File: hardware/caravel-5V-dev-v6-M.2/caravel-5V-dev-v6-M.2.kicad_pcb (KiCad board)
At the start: 2 copper layers, 76.2 x 73.8 mm, 75 parts, among them J1 USB_B_Micro - 10118193-0001LF, J10 Conn_01x02_Male, J11 Conn_01x20_Female, J12 Conn_01x27_Female, J13 Conn_01x02_Male, J2 Conn_01x02_Female, J3 Conn_01x02_Male, J4 Conn_01x03_Female, J5 Conn_01x02_Male, J6 Conn_01x02_Male, J7 Conn_01x06_Female, J8 Conn_01x02_Male, J9 Conn_01x02_Male, SW1 SW_Push - SKQGADE010, T1 Logo, T2 Logo, U1 FT232H, U10 TXB0104PWR, U2 SN74LVC1G125DCKR, U3 SN74LVC1G125DCKR, U4 MCP1319MT-29LE-OT, U5 TAR5SxxU_SOT353F, U6 TXB0104PWR, U7 W25Q32FVSS, U8 caravel-M.2-card, U9 TXB0104PWR, X1 SG7050CCN_10MHZ, Y1 CSTNE12M0GH5L000R0

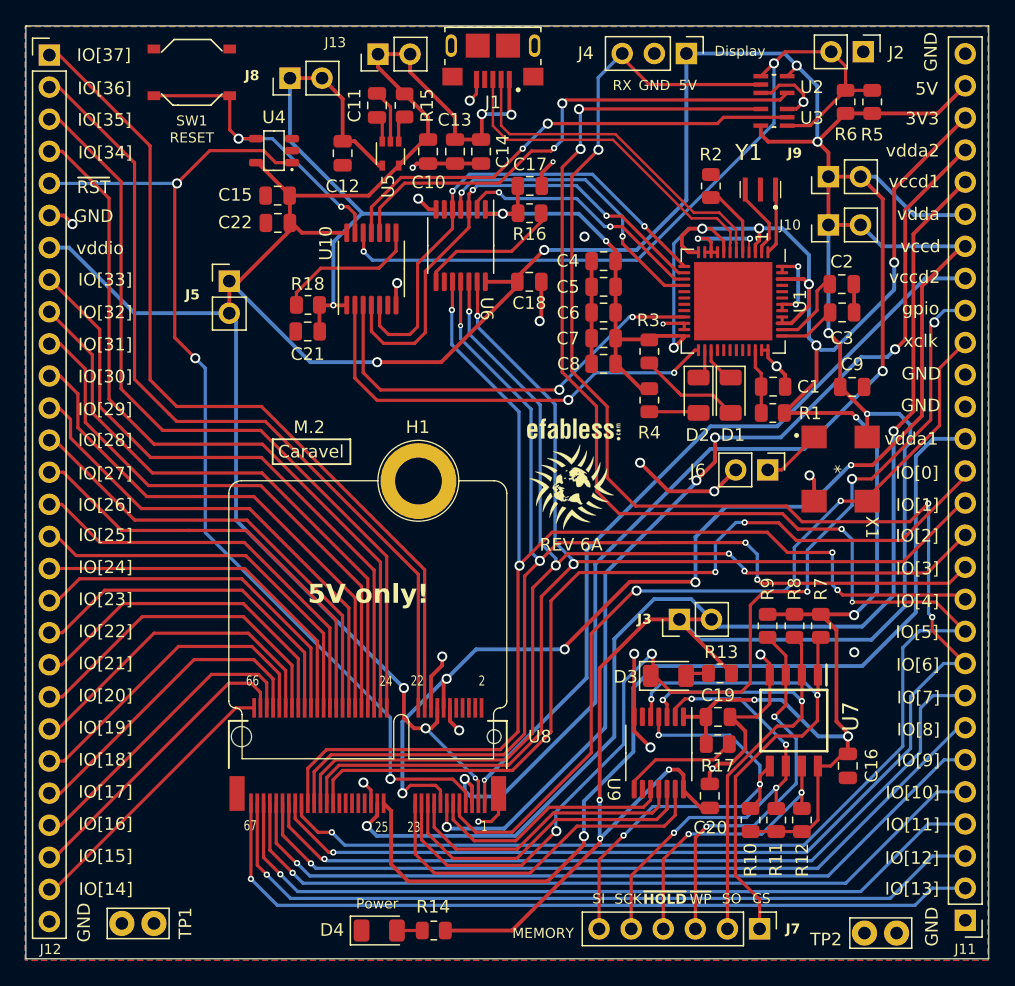
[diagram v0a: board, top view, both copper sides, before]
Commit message: update `caravel-5V-dev-v6-M.2` to REV6B that fixes identified issues during bringup
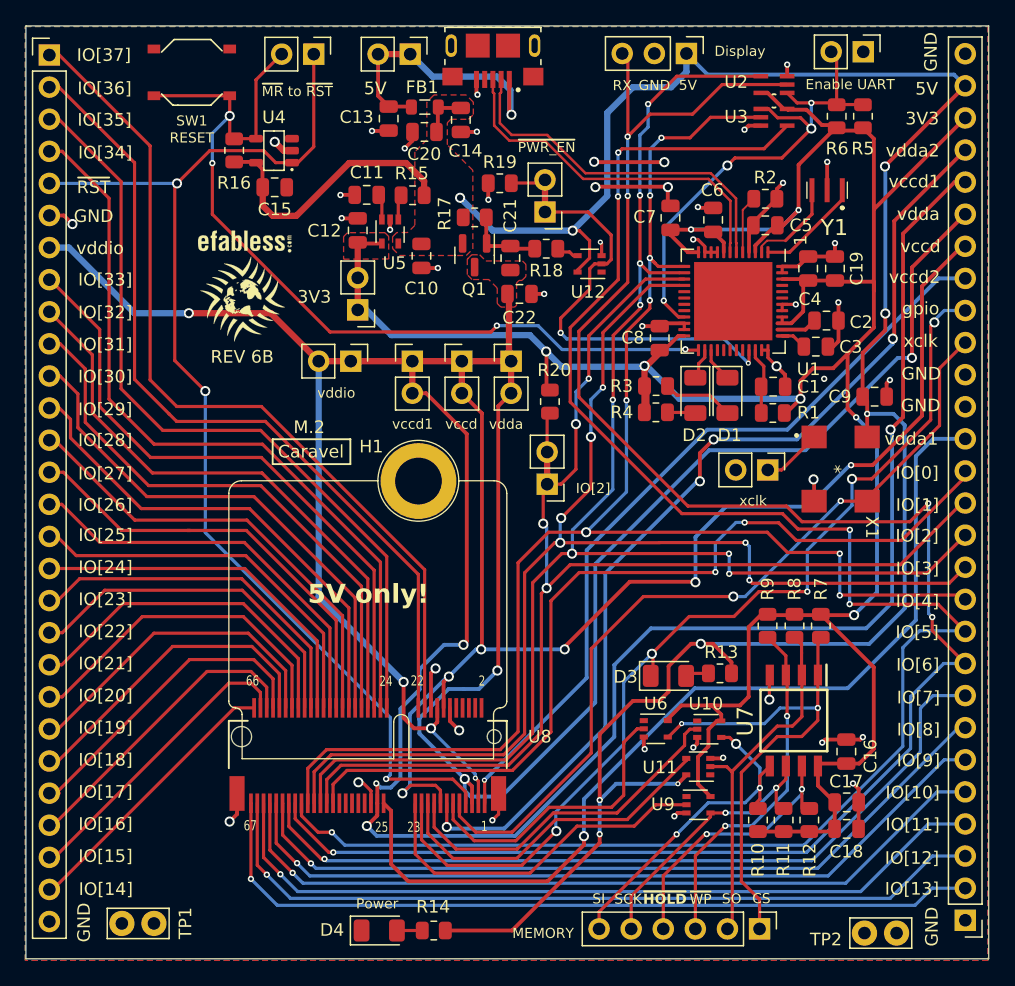
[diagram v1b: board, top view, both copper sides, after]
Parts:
- added FB1: 600R/0.5A, Inductor_SMD:L_0805_2012Metric, F.Cu at (126.6, 124.1)
- added J14: Conn_01x02_Pin, Connector_PinHeader_2.54mm:PinHeader_1x02_P2.54mm_Vertical, F.Cu at (117.8, 119.9)
- added J15: Conn_01x02_Pin, Connector_PinHeader_2.54mm:PinHeader_1x02_P2.54mm_Vertical, F.Cu at (136.1, 132.4)
- added J16: Conn_01x02_Pin, Connector_PinHeader_2.54mm:PinHeader_1x02_P2.54mm_Vertical, F.Cu at (136.3, 153.9)
- added Q1: IRLML6402, Package_TO_SOT_SMD:SOT-23, F.Cu at (130.5, 135.8)
- added R19: 10K, Resistor_SMD:R_0805_2012Metric, F.Cu at (132.5, 130.1)
- added R20: 100K, Resistor_SMD:R_0805_2012Metric, F.Cu at (136.5, 147.4)
- added U11: SN74LV1T34DCK, Package_TO_SOT_SMD:SOT-353_SC-70-5, F.Cu at (148.2, 176.3)
- added U12: SN74LV1T34DCK, Package_TO_SOT_SMD:SOT-353_SC-70-5, F.Cu at (139.6, 136.5)
- C1: value 0.01uf - CC0805JRX7R9BB103 -> 0.01uF
- C10: value 1uf - CC0805KKX5R8BB105 -> 1uf
- C11: value 0.01uf - CC0805KRX7R9BB103 -> 0.01uF
- C12: value 10uf - CC0805KKX5R8BB106 -> 10uf
- C13, C17: value 0.1uf - CC0805KRX7R9BB104 -> 0.01uF
- C14: value 10uf - CC0805KKX5R8BB106 -> 0.1uF
- C15, C16, C2, C21, C22, C3, C4, C5, C6, C7, C8, C9: value 0.1uf - CC0805KRX7R9BB104 -> 0.1uF
- C18: value 0.1uf - CC0805KRX7R9BB104 -> 1uf
- C19, C20: value 0.1uf - CC0805KRX7R9BB104 -> 10uf
- D1, D2, D3, D4: value LED - 17-215SURC/S530-A2/TR8 -> RED
- J1: value USB_B_Micro - 10118193-0001LF -> USB_B_Micro
- J10, J13, J3, J5, J6, J8, J9: value Conn_01x02_Male -> Conn_01x02_Pin
- J11: value Conn_01x20_Female -> Conn_01x28_Pin
- J12: value Conn_01x27_Female -> Conn_01x28_Pin
- J2: value Conn_01x02_Female -> Conn_01x02_Pin
- J4: value Conn_01x03_Female -> Conn_01x03_Pin
- J7: value Conn_01x06_Female -> Conn_01x06_Pin
- R1, R12, R15, R16, R17, R5, R6, R9: value 10k - RC0805FR-0710KL -> 10K
- R10, R11, R7, R8: value 10k - RC0805FR-0710KL -> 100K
- R13, R14: value 1K - RC0805FR-071KL -> 10K
- R18: value 10k - RC0805FR-0710KL -> 2K
- R2: value 12K 1% - 0805W8F1202T5E -> 12K 1%
- R3, R4: value 150 - 0805W8J0151T5E -> 150
- U10, U6, U9: value TXB0104PWR -> SN74LV1T34DCK; footprint Package_SO:TSSOP-14_4.4x5mm_P0.65mm -> Package_TO_SOT_SMD:SOT-353_SC-70-5
- U5: value TAR5SxxU_SOT353F -> TAR5SxxU
- U8: value caravel-M.2-card -> M.2-CONNECTOR-E
- Y1: value CSTNE12M0GH5L000R0 -> 12MHz
- moved C20 57.2 mm to (126.6, 126.1), turned to 0 degrees
- moved C17 54.9 mm to (160.0, 179.1)
- moved C18 50.1 mm to (160.0, 181.2), turned to 0 degrees
- moved R17 45.9 mm to (130.6, 132.8), turned to 180 degrees
- moved U10 45.2 mm to (149.1, 173.3), turned to 0 degrees
- moved U6 41.2 mm to (144.9, 173.3), turned to 0 degrees
- moved C19 36.7 mm to (159.1, 136.9), turned to 90 degrees
- moved J10 31.0 mm to (129.5, 144.2), turned to 0 degrees
- moved T2 30.0 mm to (112.3, 134.7)
- moved T1 30.0 mm to (112.1, 139.3)
- moved J3 29.4 mm to (125.6, 144.2), turned to 0 degrees
- moved J9 29.1 mm to (133.4, 144.2), turned to 0 degrees
- moved R16 23.9 mm to (111.5, 127.5), turned to 90 degrees
- moved C22 19.9 mm to (134.1, 138.9), turned to 180 degrees
- moved R18 19.4 mm to (136.2, 135.3)
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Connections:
- net FTDI_D+ renamed /FTDI_D+
- net FTDI_D- renamed /FTDI_D-
- net Net-(U1-VCCA) renamed /VCCA
- net Net-(U1-VCCCORE) renamed /VCCCORE
- net Net-(U5-Noise) renamed /Noise
- net mprj_io[0] renamed /mprj_io[0]
- net mprj_io[10] renamed /mprj_io[10]
- net mprj_io[11] renamed /mprj_io[11]
- net mprj_io[12] renamed /mprj_io[12]
- net mprj_io[13] renamed /mprj_io[13]
- net mprj_io[14] renamed /mprj_io[14]
- net mprj_io[15] renamed /mprj_io[15]
- net mprj_io[16] renamed /mprj_io[16]
- net mprj_io[17] renamed /mprj_io[17]
- net mprj_io[18] renamed /mprj_io[18]
- net mprj_io[19] renamed /mprj_io[19]
- net mprj_io[20] renamed /mprj_io[20]
- net mprj_io[21] renamed /mprj_io[21]
- net mprj_io[22] renamed /mprj_io[22]
- net mprj_io[23] renamed /mprj_io[23]
- net mprj_io[24] renamed /mprj_io[24]
- net mprj_io[25] renamed /mprj_io[25]
- net mprj_io[26] renamed /mprj_io[26]
- net mprj_io[27] renamed /mprj_io[27]
- net mprj_io[28] renamed /mprj_io[28]
- net mprj_io[29] renamed /mprj_io[29]
- net mprj_io[30] renamed /mprj_io[30]
- net mprj_io[31] renamed /mprj_io[31]
- net mprj_io[32] renamed /mprj_io[32]
- net mprj_io[33] renamed /mprj_io[33]
- net mprj_io[34] renamed /mprj_io[34]
- net mprj_io[35] renamed /mprj_io[35]
- net mprj_io[36] renamed /mprj_io[36]
- net mprj_io[37] renamed /mprj_io[37]
- net mprj_io[5]_ser_rx renamed /mprj_io[5]_ser_rx
- net mprj_io[6]_ser_tx renamed /mprj_io[6]_ser_tx
- net mprj_io[7] renamed /mprj_io[7]
- net mprj_io[8] renamed /mprj_io[8]
- net mprj_io[9] renamed /mprj_io[9]
- net vccd2 renamed /vccd2
- net vdda1 renamed /vdda1
- net vdda2 renamed /vdda2
- net xclk renamed /xclk
- net ~{MEM_HOLD} renamed /~{MEM_HOLD}
- net ~{MEM_WP} renamed /~{MEM_WP}
- net ~{RST} renamed /~{RST}
- C1 pad 2: Net-(U1-~{RESET}) -> /~{FTDI_RST}
- C10 pad 2: vccd -> +5V
- C12 pad 2: +3.3V -> +3V3
- C13 pad 1: vccd -> VBUS
- C14 pad 2: vccd -> +5V
- C15 pad 1: GND -> +5V
- C15 pad 2: vccd -> GND
- C16 pad 1: +3.3V -> +3V3
- C17 pad 2: +3.3V -> +3V3
- C18 pad 1: GND -> +3V3
- C18 pad 2: vccd -> GND
- C19 pad 1: GND -> +3V3
- C19 pad 2: +3.3V -> GND
- C20 pad 2: vccd -> +5V
- C21 pad 1: GND -> Net-(Q1-G)
- C21 pad 2: +3.3V -> VCC
- C22 pad 2: vccd -> VCC
- C4 pad 1: GND -> +3V3
- C4 pad 2: +3.3V -> GND
- C5 pad 1: GND -> +3V3
- C5 pad 2: +3.3V -> GND
- C6 pad 1: GND -> +3V3
- C6 pad 2: +3.3V -> GND
- C7 pad 1: GND -> +3V3
- C7 pad 2: +3.3V -> GND
- C8 pad 1: GND -> +3V3
- C8 pad 2: +3.3V -> GND
- C9 pad 2: vccd -> +5V
- J1 pad 1: vccd -> VBUS
- J10 pad 1: vccd -> VCC
- J10 pad 2: vccd -> VCC
- J11 pad 11: mprj_io[4]_SCK -> /USB_SCK_TXD
- J11 pad 12: mprj_io[3]_CSB -> /USB_CS1
- J11 pad 13: mprj_io[2]_SDI -> /USB_SO_RXD
- J11 pad 14: mprj_io[1]_SDO -> /USB_SI
- J11 pad 22: vccd -> VCC
- J11 pad 23: vccd -> VCC
- J11 pad 24: vccd -> VCC
- J11 pad 26: +3.3V -> +3V3
- J11 pad 27: vccd -> +5V
- J12 pad 7: vccd -> VCC
- J13 pad 1: vccd -> VBUS
- J13 pad 2: vccd -> VBUS
- J2 pad 2: UART_EN -> /~{UART_EN}
- J3 pad 1: vccd -> VCC
- J3 pad 2: vccd -> VCC
- J4 pad 1: vccd -> +5V
- J5 pad 1: vccd -> VCC
- J5 pad 2: vccd -> VCC
- J7 pad 1: MEM_CS -> /~{MEM_CS}
- J7 pad 2: MEM_SO -> /MEM_SO
- J7 pad 5: MEM_SCK -> /MEM_SCK
- J7 pad 6: MEM_SI -> /MEM_SI
- J8 pad 1: +3.3V -> +3V3
- J8 pad 2: +3.3V -> +3V3
- J9 pad 1: vccd -> VCC
- J9 pad 2: vccd -> VCC
- R1 pad 1: Net-(U1-~{RESET}) -> +3V3
- R1 pad 2: +3.3V -> /~{FTDI_RST}
- R10 pad 1: MEM_SI -> /MEM_SI
- R10 pad 2: +3.3V -> +3V3
- R11 pad 1: MEM_SCK -> /MEM_SCK
- R11 pad 2: +3.3V -> +3V3
- R12 pad 2: +3.3V -> +3V3
- R13 pad 1: vccd -> +5V
- R14 pad 1: vccd -> +5V
- R15 pad 2: vccd -> +5V
- R16 pad 1: +3.3V -> +5V
- R16 pad 2: Net-(U6-OE) -> /~{MR}
- R17 pad 1: +3.3V -> Net-(Q1-G)
- R17 pad 2: Net-(U9-OE) -> +5V
- R18 pad 1: +3.3V -> /~{PWR_EN}_H
- R18 pad 2: Net-(U10-OE) -> Net-(Q1-G)
- R3 pad 2: +3.3V -> +3V3
- R4 pad 2: +3.3V -> +3V3
- R5 pad 1: vccd -> +3V3
- R5 pad 2: UART_EN -> /~{UART_EN}
- R6 pad 1: vccd -> +3V3
- R6 pad 2: UART_EN -> /~{UART_EN}
- R7 pad 1: MEM_CS -> /~{MEM_CS}
- R7 pad 2: +3.3V -> +3V3
- R8 pad 1: MEM_SO -> /MEM_SO
- R8 pad 2: +3.3V -> +3V3
- R9 pad 2: +3.3V -> +3V3
- SW1 pad 1: ~{MR} -> /~{MR}
- U1 pad 12: +3.3V -> +3V3
- U1 pad 13: USB_SCK_TXD -> /USB_SCK_TXD
- U1 pad 14: USB_SO_RXD -> /USB_SO_RXD
- U1 pad 15: USB_SI -> /USB_SI
- U1 pad 16: USB_CS1 -> /USB_CS1
- U1 pad 21: UART_EN_L -> /~{UART_EN}
- U1 pad 24: +3.3V -> +3V3
- U1 pad 25: ~{MR}_L -> /~{MR}
- U1 pad 3: +3.3V -> +3V3
- U1 pad 33: unconnected-(U1-ACBUS9-Pad33) -> /~{PWR_EN}
- U1 pad 34: Net-(U1-~{RESET}) -> /~{FTDI_RST}
- U1 pad 39: +3.3V -> +3V3
- U1 pad 40: +3.3V -> +3V3
- U1 pad 46: +3.3V -> +3V3
- U1 pad 8: +3.3V -> +3V3
- U10 pad 1: +3.3V -> unconnected-(U10-NC-Pad1)
- U10 pad 2: ~{MR}_L -> /Caravel_D0
- U10 pad 3: UART_EN_L -> GND
- U10 pad 4: USB_SO_RXD -> /MEM_SI
- U10 pad 5: USB_SCK_TXD -> +3V3
- U2 pad 1: UART_EN -> /~{UART_EN}
- U2 pad 4: USB_SO_RXD_H -> /USB_SO_RXD
- U2 pad 5: vccd -> +3V3
- U3 pad 1: UART_EN -> /~{UART_EN}
- U3 pad 2: USB_SCK_TXD_H -> /USB_SCK_TXD
- U3 pad 5: vccd -> +3V3
- U4 pad 4: ~{MR} -> /~{MR}
- U4 pad 5: vccd -> +5V
- U5 pad 4: +3.3V -> +3V3
- U5 pad 5: vccd -> +5V
- U6 pad 1: +3.3V -> unconnected-(U6-NC-Pad1)
- U6 pad 2: USB_SI -> /Caravel_CSB
- U6 pad 3: USB_SO_RXD -> GND
- U6 pad 4: USB_CS1 -> /~{MEM_CS}
- U6 pad 5: USB_SCK_TXD -> +3V3
- U7 pad 1: MEM_CS -> /~{MEM_CS}
- U7 pad 2: MEM_SO -> /MEM_SO
- U7 pad 5: MEM_SI -> /MEM_SI
- U7 pad 6: MEM_SCK -> /MEM_SCK
- U7 pad 8: +3.3V -> +3V3
- U8 pad 11: Caravel_CSB -> /Caravel_CSB
- U8 pad 14: vccd -> VCC
- U8 pad 15: vccd -> VCC
- U8 pad 16: vccd -> VCC
- U8 pad 17: Caravel_D0 -> /Caravel_D0
- U8 pad 19: Caravel_D1 -> /Caravel_D1
- U8 pad 23: Caravel_SCK -> /Caravel_SCK
- U8 pad 3: vccd -> VCC
- U8 pad 35: vccd -> VCC
- U8 pad 5: vccd -> VCC
- U8 pad 51: mprj_io[1]_SDO -> /USB_SI
- U8 pad 53: mprj_io[2]_SDI -> /USB_SO_RXD
- U8 pad 55: mprj_io[3]_CSB -> /USB_CS1
- U8 pad 57: mprj_io[4]_SCK -> /USB_SCK_TXD
- U9 pad 1: +3.3V -> unconnected-(U9-NC-Pad1)
- U9 pad 2: MEM_SCK -> /Caravel_SCK
- U9 pad 3: MEM_SO -> GND
- U9 pad 4: MEM_SI -> /MEM_SCK
- U9 pad 5: MEM_CS -> +3V3
- X1 pad 4: vccd -> +5V
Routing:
- net vccd: track 614.9 -> 0.00 mm, vias 23 -> 0
- net VCC: track 0.00 -> 438.1 mm, vias 0 -> 17
- net +3V3: track 0.00 -> 230.9 mm, vias 0 -> 7
- net +3.3V: track 229.3 -> 0.00 mm, vias 13 -> 0
- net +5V: track 0.00 -> 197.0 mm, vias 0 -> 9
- net /USB_SO_RXD: track 0.00 -> 121.7 mm, vias 0 -> 8
- net /USB_SCK_TXD: track 0.00 -> 120.3 mm, vias 0 -> 8
- net /USB_SI: track 0.00 -> 105.0 mm, vias 0 -> 4
- net mprj_io[4]_SCK: track 98.6 -> 0.00 mm, vias 4 -> 0
- net /USB_CS1: track 0.00 -> 98.1 mm, vias 0 -> 6
- net mprj_io[3]_CSB: track 96.6 -> 0.00 mm, vias 4 -> 0
- net mprj_io[2]_SDI: track 94.5 -> 0.00 mm, vias 4 -> 0
- net mprj_io[1]_SDO: track 93.2 -> 0.00 mm, vias 2 -> 0
- net /~{MR}: track 0.00 -> 70.4 mm, vias 0 -> 4
- net UART_EN: track 61.3 -> 0.00 mm, vias 2 -> 0
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- added copper zone on F.Cu, net +3V3
- added copper zone on F.Cu, net +5V
- added copper zone on F.Cu, net VCC
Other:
- board text added: "Enable UART"
- board text added: "REV 6B"
- board text added: "~{MR} to ~{RST}"
- board text added: "~{PWR_EN}"
- board text removed: "REV 6A"

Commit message: update `caravel-5V-dev-v6-M.2` (REV6B) pcb and gerber files
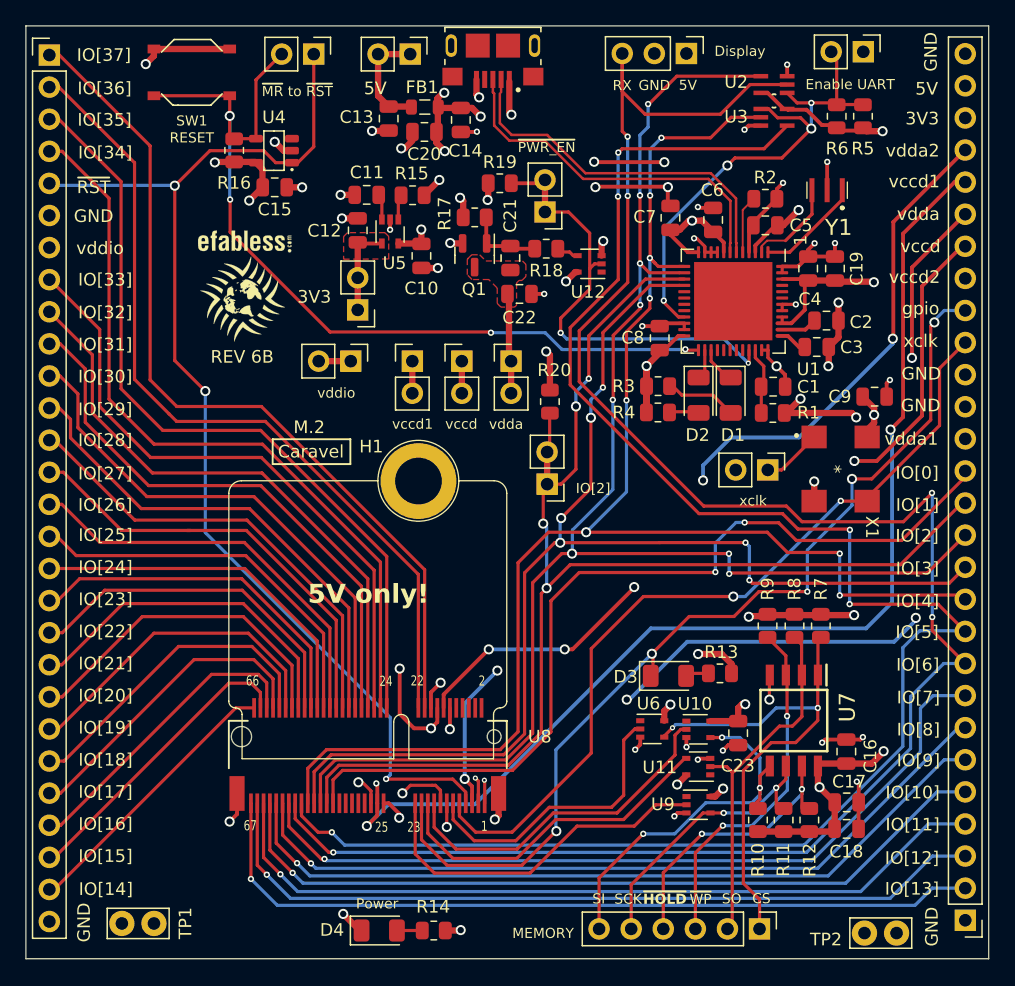
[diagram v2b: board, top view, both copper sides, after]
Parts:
- added C23: 0.1uF, Capacitor_SMD:C_0805_2012Metric, F.Cu at (151.4, 173.7)
- moved U10 0.86 mm to (148.2, 173.3)
- moved U6 0.28 mm to (144.6, 173.3)
- moved D2 0.26 mm to (148.3, 146.9)
- moved D1 0.26 mm to (150.8, 146.9)
- moved R4 0.16 mm to (145.1, 148.3)
- moved R3 0.16 mm to (145.1, 146.2)
- moved C3 0.08 mm to (157.6, 143.1)
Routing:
- net +5V: track 197.0 -> 34.2 mm, vias 9 -> 14
- net +3V3: track 230.9 -> 260.7 mm, vias 7 -> 15
- net GND: track 94.5 -> 106.2 mm, vias 44 -> 48
- net VCC: track 438.1 -> 428.0 mm, vias 17 -> 14
- net /vdda1: track 75.3 -> 70.4 mm, vias 1 -> 3
- net /mprj_io[6]_ser_tx: track 153.5 -> 157.5 mm
- net /MEM_SI: track 27.8 -> 31.0 mm
- net /~{PWR_EN}: track 38.9 -> 36.5 mm
- net /~{MR}: track 70.4 -> 68.9 mm
- net /vdda2: track 79.3 -> 78.1 mm, vias 4 -> 3
- net /mprj_io[5]_ser_rx: track 144.0 -> 143.2 mm
- added copper zone on In2.Cu, net +5V
- added copper zone on In1.Cu, net GND
- removed copper zone on F.Cu, net +5V
- removed copper zone on B.Cu, net GND
- removed copper zone on F.Cu, net GND
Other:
- copper layers 2 -> 4
